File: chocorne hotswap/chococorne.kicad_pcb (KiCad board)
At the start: 2 copper layers, 261.7 x 87.7 mm, 112 parts, among them J1 MJ-4PP-9, J2 OLED, SW1 SW_PUSH, SW10 SW_PUSH, SW11 SW_PUSH, SW12 SW_PUSH, SW13 SW_PUSH, SW14 SW_PUSH, SW15 SW_PUSH, SW16 SW_PUSH, SW17 SW_PUSH, SW18 SW_PUSH, SW19 SW_PUSH, SW2 SW_PUSH, SW20 SW_PUSH, SW21 SW_PUSH, SW3 SW_PUSH, SW4 SW_PUSH, SW5 SW_PUSH, SW6 SW_PUSH, SW7 SW_PUSH, SW8 SW_PUSH, SW9 SW_PUSH, U1 ProMicro

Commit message: chocorne: bump version
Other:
- board text added: "6f389fa"
- board text removed: "52d4260"

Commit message: chocorne: move holes to m2 spacers footprint
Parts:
- ? (x2): value M2_HOLE_NPH -> M2_SPACER; footprint holykeebs:M2_HOLE_NPH -> holykeebs:M2_SPACER
- SW1 (x2), SW10 (x2), SW11 (x2), SW12 (x2), SW13 (x2), SW14 (x2), SW15 (x2), SW16 (x2), SW17 (x2), SW18 (x2), SW19 (x2), SW2 (x2), SW20 (x2), SW21 (x2), SW3 (x2), SW4 (x2), SW5 (x2), SW6 (x2), SW7 (x2), SW8 (x2), SW9 (x2): footprint keyswitches:Kailh_socket_PG1350_optional_oval_alternate_pinout -> keyswitches:Kailh_socket_PG1350_optional_oval_smaller_hotswap_alternate_pinout
- h2 (x8): footprint holykeebs:M2_HOLE_NPH -> holykeebs:M2_SPACER
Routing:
- net col5: track 251.3 -> 246.4 mm
- net row0: track 339.0 -> 339.7 mm

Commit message: chocorne: bump version
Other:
- board text added: "7b9e311"
- board text removed: "6f389fa"

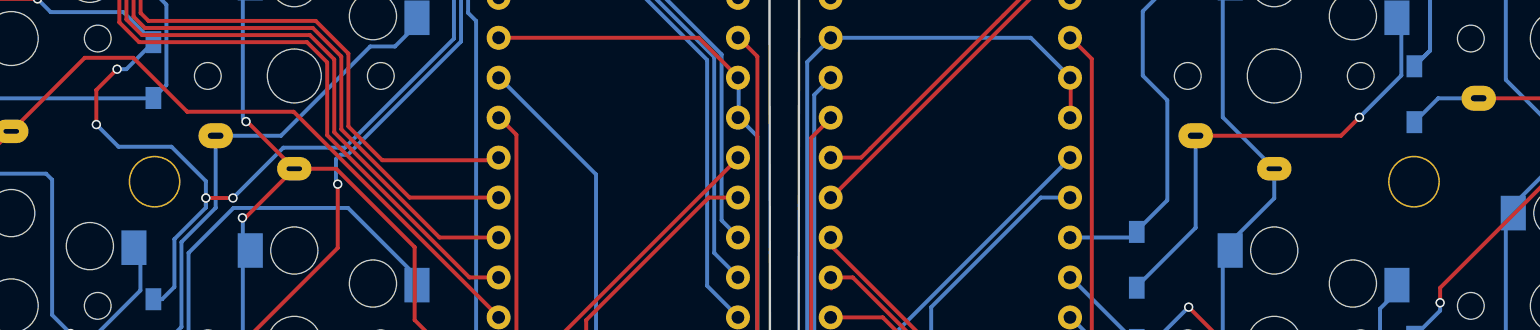
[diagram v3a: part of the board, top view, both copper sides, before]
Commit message: chocorne: move top right mounting hole so screw head doesn't hit the switch edge
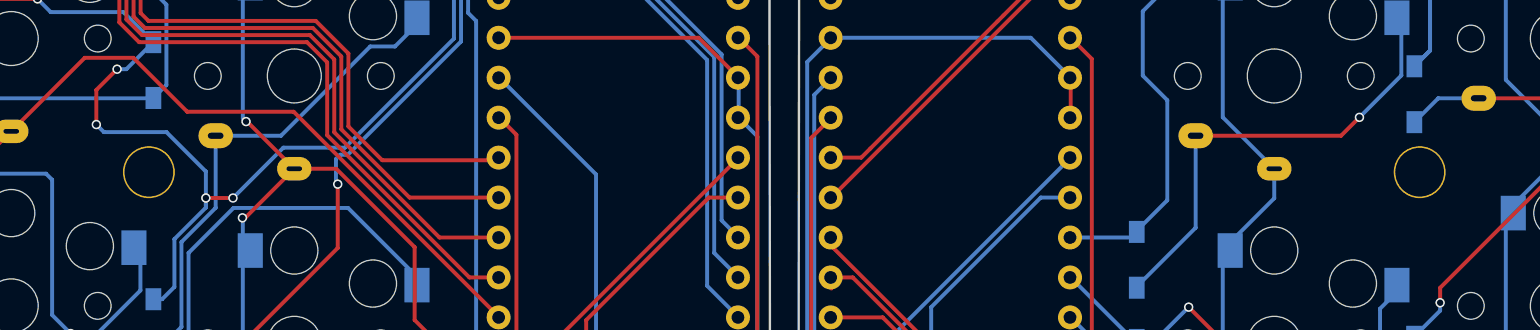
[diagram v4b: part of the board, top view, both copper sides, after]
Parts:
- ?: moved to B.Cu
- moved ? 0.71 mm to (188.1, 72.0)
- moved ? 0.71 mm to (107.3, 72.0), turned to 180 degrees

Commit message: chocorne: bump version
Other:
- board text added: "8c8d947"
- board text removed: "7b9e311"

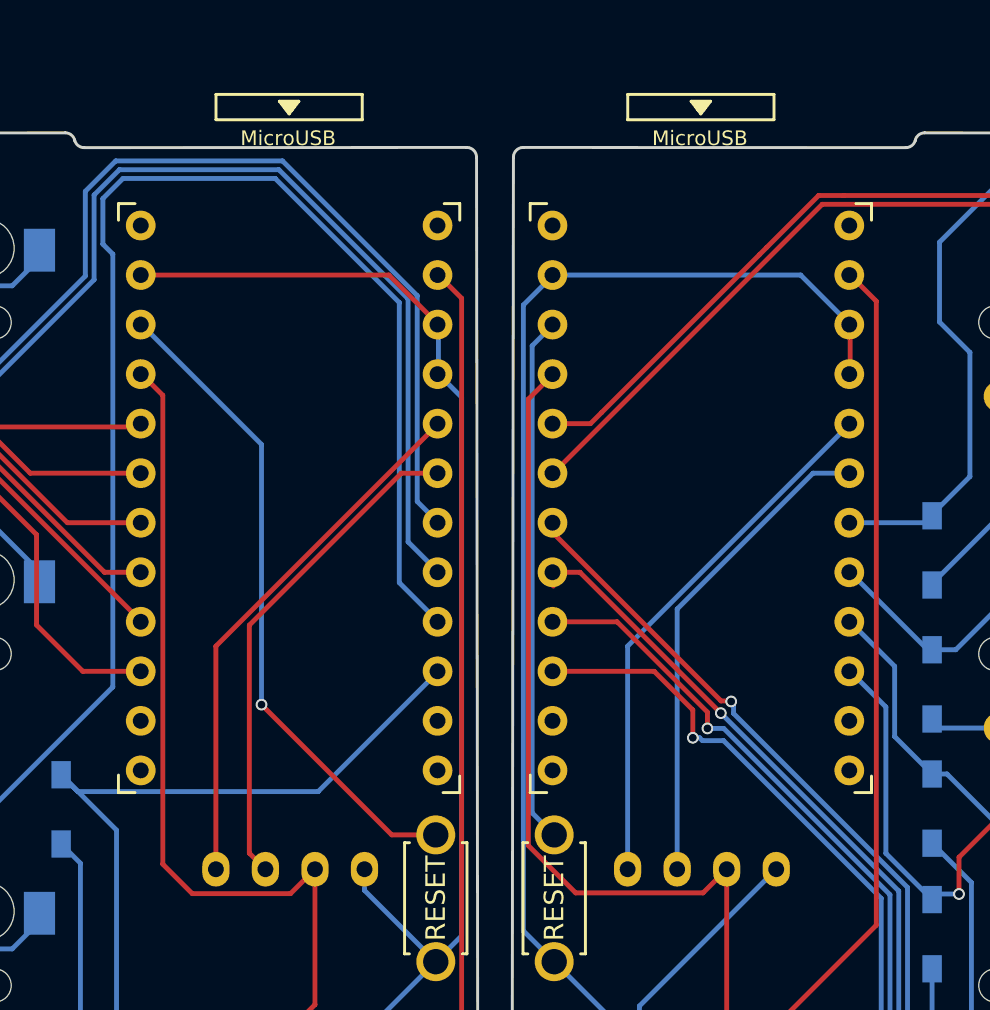
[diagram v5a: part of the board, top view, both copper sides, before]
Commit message: corne choc: enlarge holes to 1mm
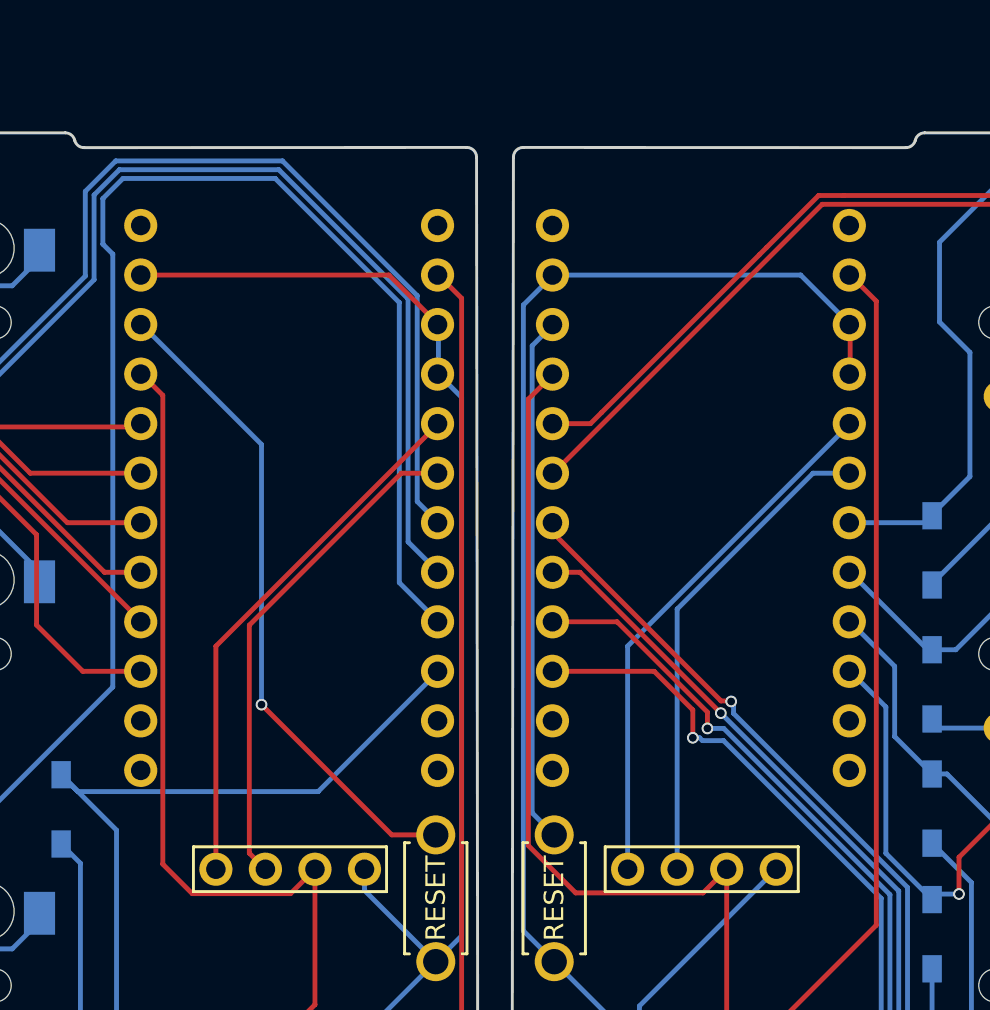
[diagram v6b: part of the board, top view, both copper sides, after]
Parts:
- J2 (x2): footprint kbd:OLED_1side -> holykeebs:OLED_1side_1mm_holes
- U1 (x2): footprint kbd:ProMicro_v3 -> holykeebs:ProMicro_1mm_holes

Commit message: corne choc: bump version
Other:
- board text added: "03ac5ed"
- board text removed: "8c8d947"
